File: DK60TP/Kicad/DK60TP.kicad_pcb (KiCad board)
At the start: 2 copper layers, 285.1 x 113.1 mm, 161 parts, among them J1 USB_mini_micro_B, K1 K00, K10 K09, K11 K0A, K12 K0B, K13 K0C, K14 K10, K15 K11, K16 K12, K17 K13, K18 K14, K19 K15, K2 K01, K20 K16, K21 K17, K22 K18, K23 K19, K24 K1A, K25 K1B, K26 K1C, K27 K20, K28 K21, K29 K22, K3 K02, K30 K23, K31 K24, K32 K25, K33 K26, K34 K27, K35 K28, K36 K29, K37 K2A, K38 K2B, K39 K2C, K4 K03, K40 K30, K41 K31, K42 K32, K43 K33, K44 K34, K45 K35, K46 K36, K47 K37, K48 K38, K49 K39, K5 K04, K50 K3A, K51 K3B, K52 K3C, K53 K41, K54 K42, K55 K45, K56 K48, K57 K49, K58 K4A, K59 K4B, K6 K05, K60 K4C, K61 Ctrl, K62 K43, K63 K44, K64 K46, K65 K45, K7 K06, K8 K07, K9 K08, SW1 SW_PUSH, U0 ATMEGA32U4, X1 XTAL_GND

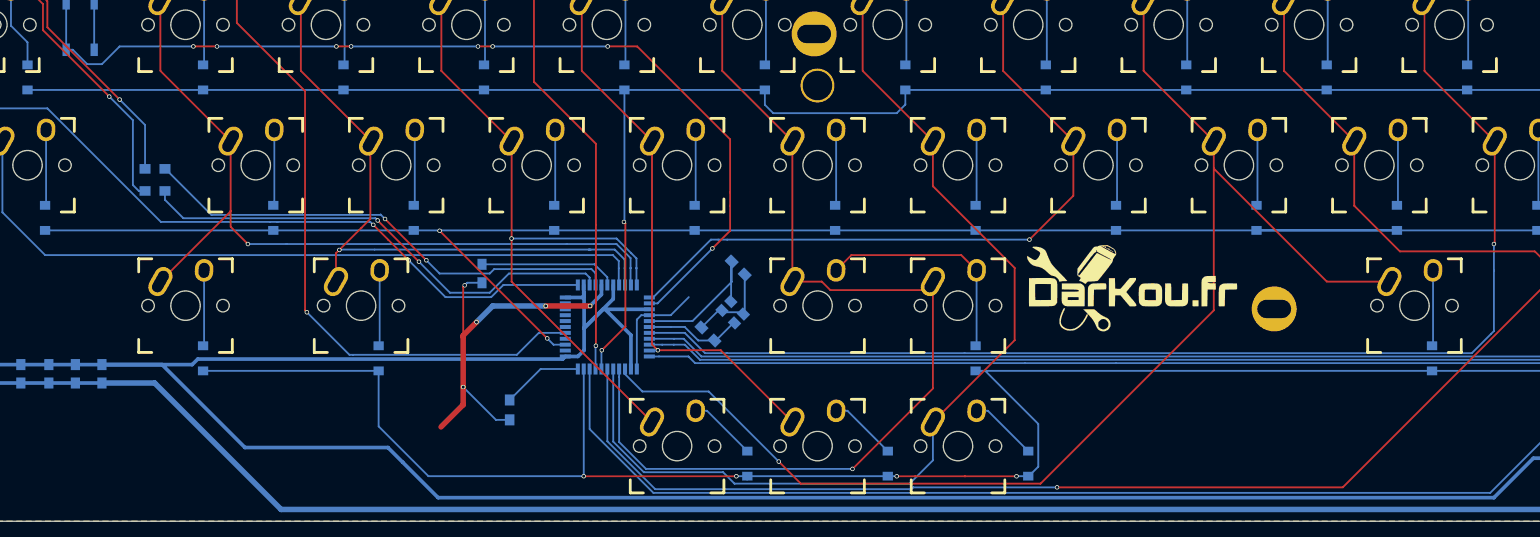
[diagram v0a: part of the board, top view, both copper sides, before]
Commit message: - DK60TP: Changed rows/cols assignation to  simplify routing
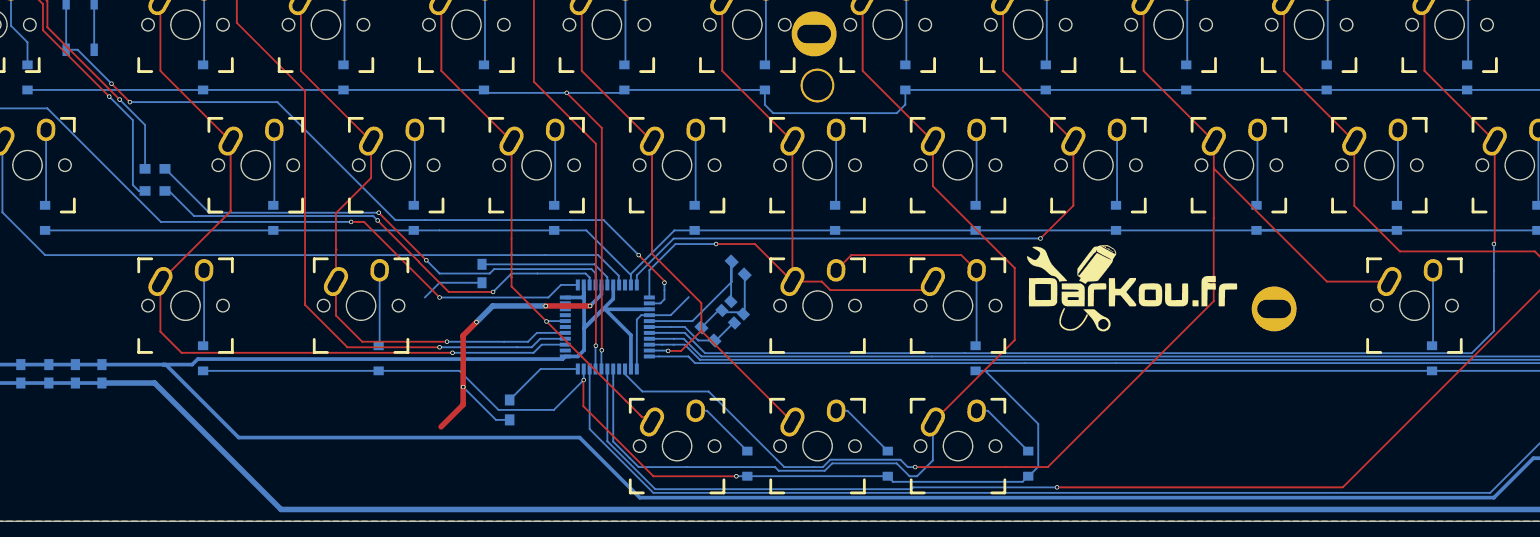
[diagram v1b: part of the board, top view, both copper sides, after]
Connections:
- U0 pad 10: /Col1 -> /Row3
- U0 pad 11: /Col3 -> /Col7
- U0 pad 12: /Col7 -> /Col5
- U0 pad 26: /Col5 -> Net-(U0-Pad26)
- U0 pad 36: /Row3 -> /Col1
- U0 pad 37: Net-(U0-Pad37) -> /Row0
- U0 pad 38: /Row0 -> /Col2
- U0 pad 40: Net-(U0-Pad40) -> /Col3
- U0 pad 9: /Col2 -> Net-(U0-Pad9)
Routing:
- net /Col5: track 179.1 -> 133.3 mm
- net Net-(R1-Pad2): track 136.9 -> 111.3 mm, vias 8 -> 4
- net /Col3: track 134.7 -> 116.0 mm
- net /Row3: track 291.3 -> 274.2 mm, vias 2 -> 0
- net /Row4: track 374.0 -> 362.4 mm, vias 4 -> 2
- net VCC: track 489.8 -> 481.5 mm
- net /Col2: track 131.1 -> 126.0 mm
- net /Col7: track 137.6 -> 140.3 mm
- net /Col4: track 119.2 -> 121.2 mm
- net /Col8: track 216.6 -> 214.8 mm
- net /Row0: track 351.1 -> 349.4 mm
- net /Col1: track 151.9 -> 153.4 mm
- net /Col0: track 161.3 -> 160.2 mm
- net GND: track 447.2 -> 446.2 mm, vias 12 -> 11
- net Net-(R3-Pad1): track 66.3 -> 65.6 mm

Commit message: - Rewrote all for DK60TP
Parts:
- removed D20: D16, Footprint:D_SOD123
- removed D25: D1B, Footprint:D_SOD123
- removed D30: D23, Footprint:D_SOD123
- removed G*** (x2): LOGO, Footprint:darkou
- removed G***: LOGO, Footprint:OPEN-HARDWARE
- removed K25: K1B, Footprint:Mx_Alps_100
- removed K26: K1C, Footprint:Mx_Alps_100
- removed K31: K24, Footprint:Mx_Alps_100
- removed K36: K29, Footprint:Mx_Alps_100
- removed K37: K2A, Footprint:Mx_Alps_100
- removed P?: CONN_1, Footprint:PIN_1
- removed the Poker_oval_hole at (91.8, 127.4)
- removed the Poker_oval_hole at (194.8, 146.5)
- removed the Poker_oval_hole at (326.8, 127.5)
- removed the Poker_oval_hole at (257.2, 183.8)
- removed the Poker_side_edge_long at (351.7, 156.0)
- removed the Poker_side_edge_long at (66.6, 156.0)
- added D64: D, Footprint:D_SOD123, B.Cu at (296.5, 38.0)
- added D65: D, Footprint:D_SOD123, B.Cu at (289.2, 58.8)
- added D66: D, Footprint:D_SOD123, B.Cu at (294.5, 77.5)
- added D67: D, Footprint:D_SOD123, B.Cu at (307.5, 95.0)
- added D68: D, Footprint:D_SOD123, B.Cu at (309.0, 111.8)
- added K66: K1B, Footprint:Mx_Alps_100, F.Cu at (257.2, 50.0)
- added K67: K2B, Footprint:Mx_Alps_100, F.Cu at (261.9, 69.1)
- added K68: K3B, Footprint:Mx_Alps_100, F.Cu at (252.4, 88.1)
- added K69: K4B, Footprint:Mx_Alps_100, F.Cu at (257.2, 107.2)
- added K70: K4B, Footprint:Mx_Alps_125, F.Cu at (254.8, 107.2)
- added K71: K4B, Footprint:Mx_Alps_150, F.Cu at (252.4, 107.2)
- added K72: K0C, Footprint:Mx_Alps_100, F.Cu at (266.7, 31.0)
- added K73: K1C, Footprint:Mx_Alps_100, F.Cu at (276.2, 50.0)
- added K74: K2C, Footprint:Mx_Alps_100, F.Cu at (281.0, 69.1)
- added K75: K3C, Footprint:Mx_Alps_275, F.Cu at (288.1, 88.1)
- added K76: K4C, Footprint:Mx_Alps_100, F.Cu at (276.2, 107.2)
- added K77: K4C, Footprint:Mx_Alps_125, F.Cu at (278.6, 107.2)
- added K78: K0D, Footprint:Mx_Alps_100, F.Cu at (285.8, 31.0)
- added K79: K0D, Footprint:Mx_Alps_200, F.Cu at (295.3, 31.0)
- added K80: K1D, Footprint:Mx_Alps_150, F.Cu at (300.0, 50.0)
- added K81: K2D, Footprint:Mx_Alps_225, F.Cu at (292.9, 69.1)
- added K82: K1D, Footprint:Mx_Alps_200, F.Cu at (302.4, 59.5)
- added K83: K3D, Footprint:Mx_Alps_100, F.Cu at (304.8, 88.1)
- added K84: K3C, Footprint:Mx_Alps_175, F.Cu at (278.6, 88.1)
- added K85: K4D, Footprint:Mx_Alps_125, F.Cu at (302.4, 107.2)
- added K86: K4D, Footprint:Mx_Alps_150, F.Cu at (300.0, 107.2)
- added MXST: VAL**, Footprint:MXST, F.Cu at (114.3, 107.2)
- added MXST: VAL**, Footprint:MXST, F.Cu at (304.8, 69.1)
- added MXST: VAL**, Footprint:MXST, F.Cu at (307.2, 31.0)
- added MXST: VAL**, Footprint:MXST, F.Cu at (283.4, 31.0)
- added MXST: VAL**, Footprint:MXST, F.Cu at (61.9, 88.1)
- added MXST: VAL**, Footprint:MXST, F.Cu at (38.1, 88.1)
- added MXST: VAL**, Footprint:MXST, F.Cu at (228.6, 107.2)
- added MXST: VAL**, Footprint:MXST, F.Cu at (209.6, 107.2)
- added MXST: VAL**, Footprint:MXST, F.Cu at (109.5, 107.2)
- added MXST: VAL**, Footprint:MXST, F.Cu at (300.0, 88.1)
- added MXST: VAL**, Footprint:MXST, F.Cu at (276.2, 88.1)
- added MXST: VAL**, Footprint:MXST, F.Cu at (302.4, 47.6)
- added MXST: VAL**, Footprint:MXST, F.Cu at (302.4, 71.4)
- added MXST: VAL**, Footprint:MXST, F.Cu at (281.0, 69.1)
- added P1: CONN_01X04, Pin_Headers:Pin_Header_Angled_1x04, B.Cu at (202.8, 104.8)
- added Poker_oval_hole: VAL**, Footprint:Poker_oval_hole, F.Cu at (289.1, 49.8)
- added Poker_oval_hole: VAL**, Footprint:Poker_oval_hole, F.Cu at (157.2, 68.9)
- added Poker_oval_hole: VAL**, Footprint:Poker_oval_hole, F.Cu at (219.5, 107.1)
- added Poker_side_edge_long: VAL**, Footprint:Poker_side_edge_long, F.Cu at (314.0, 78.4)
- added Poker_side_edge_long: VAL**, Footprint:Poker_side_edge_long, F.Cu at (29.0, 78.4)
- added REF**: MountingHole_2.2mm_M2_Pad, Mounting_Holes:MountingHole_2.2mm_M2_Pad, F.Cu at (157.2, 78.6)
- added REF**: MountingHole_2.2mm_M2_Pad, Mounting_Holes:MountingHole_2.2mm_M2_Pad, F.Cu at (54.2, 49.8)
- D1: value D00 -> D
- D10: value D09 -> D
- D11: value D0A -> D
- D12: value D0B -> D
- D13: value D0C -> D
- D14: value D10 -> D
- D15: value D11 -> D
- D16: value D12 -> D
- D17: value D13 -> D
- D18: value D14 -> D
- D19: value D15 -> D
- D2: value D01 -> D
- D21: value D17 -> D
- D22: value D18 -> D
- D23: value D19 -> D
- D24: value D1A -> D
- D26: value D1C -> D
- D27: value D20 -> D
- D28: value D21 -> D
- D29: value D22 -> D
- D3: value D02 -> D
- D31: value D24 -> D
- D32: value D25 -> D
- D33: value D26 -> D
- D34: value D27 -> D
- D35: value D28 -> D
- D36: value D29 -> D
- D37: value D2A -> D
- D38: value D2B -> D
- D39: value D2C -> D
- D4: value D03 -> D
- D40: value D30 -> D
- D41: value D31 -> D
- D42: value D32 -> D
- D43: value D33 -> D
- D44: value D34 -> D
- D45: value D35 -> D
- D46: value D36 -> D
- D47: value D37 -> D
- D48: value D38 -> D
- D49: value D39 -> D
- D5: value D04 -> D
- D50: value D3A -> D
- D51: value D3B -> D
- D52: value D3C -> D
- D53: value D41 -> D
- D54: value D42 -> D
- D55: value D45 -> D
- D56: value D48 -> D
- D57: value D49 -> D
- D58: value D4A -> D
- D59: value D4B -> D
- D6: value D05 -> D
- D60: value D4C -> D
- D61: value D43 -> D
- D62: value D44 -> D
- D63: value D46 -> D
- D7: value D06 -> D
- D8: value D07 -> D
- D9: value D08 -> D
- K10: value K09 -> K11
- K11: value K0A -> K21
- K12: value K0B -> K31
- K13: value K0C -> K41; footprint Footprint:Mx_Alps_100 -> Footprint:Mx_Alps_125
- K14: value K10 -> K41; footprint Footprint:Mx_Alps_150 -> Footprint:Mx_Alps_100
- K15: value K11 -> K02
- K17: value K13 -> K22
- K18: value K14 -> K32
- K19: value K15 -> K42; footprint Footprint:Mx_Alps_100 -> Footprint:Mx_Alps_125
- K2: value K01 -> K10; footprint Footprint:Mx_Alps_100 -> Footprint:Mx_Alps_150
- K20: value K16 -> K42; footprint Footprint:Mx_Alps_100 -> Footprint:Mx_Alps_150
- K21: value K17 -> K03
- K22: value K18 -> K13
- K23: value K19 -> K23
- K24: value K1A -> K33
- K27: value K20 -> K04; footprint Footprint:Mx_Alps_175 -> Footprint:Mx_Alps_100
- K28: value K21 -> K14
- K29: value K22 -> K24
- K3: value K02 -> K20; footprint Footprint:Mx_Alps_100 -> Footprint:Mx_Alps_175
- K30: value K23 -> K34
- K32: value K25 -> K05
- K33: value K26 -> K15
- K34: value K27 -> K25
- K35: value K28 -> K35
- K38: value K2B -> K06
- K39: value K2C -> K16; footprint Footprint:Mx_Alps_225 -> Footprint:Mx_Alps_100
- K4: value K03 -> K20; footprint Footprint:Mx_Alps_100 -> Footprint:Mx_Alps_175_STEPPED
- K40: value K30 -> K26; footprint Footprint:Mx_Alps_225 -> Footprint:Mx_Alps_100
- K41: value K31 -> K36
- K42: value K32 -> K46; footprint Footprint:Mx_Alps_100 -> Footprint:Mx_Alps_600
- K43: value K33 -> K46
- K44: value K34 -> K46; footprint Footprint:Mx_Alps_100 -> Footprint:Mx_Alps_625
- K45: value K35 -> K46; footprint Footprint:Mx_Alps_100 -> Footprint:Mx_Alps_700
- K46: value K36 -> K07
- K47: value K37 -> K17
- K48: value K38 -> K27
- K49: value K39 -> K37
- K5: value K04 -> K30; footprint Footprint:Mx_Alps_100 -> Footprint:Mx_Alps_225
- K50: value K3A -> K08
- K51: value K3B -> K18; footprint Footprint:Mx_Alps_175 -> Footprint:Mx_Alps_100
- K52: value K3C -> K28
- K53: value K41 -> K38
- K54: value K42 -> K09; footprint Footprint:Mx_Alps_150 -> Footprint:Mx_Alps_100
- K55: value K45 -> K19; footprint Footprint:Mx_Alps_600 -> Footprint:Mx_Alps_100
- K56: value K48 -> K29; footprint Footprint:Mx_Alps_150 -> Footprint:Mx_Alps_100
- K57: value K49 -> K39
- K58: value K4A -> K49
- K59: value K4B -> K0A
- K6: value K05 -> K30; footprint Footprint:Mx_Alps_100 -> Footprint:Mx_Alps_125
- K60: value K4C -> K1A; footprint Footprint:Mx_Alps_150 -> Footprint:Mx_Alps_100
- K61: value Ctrl -> K2A; footprint Footprint:Mx_Alps_175_STEPPED -> Footprint:Mx_Alps_100
- K62: value K43 -> K3A
- K63: value K44 -> K4A; footprint Footprint:Mx_Alps_100 -> Footprint:Mx_Alps_125
- K64: value K46 -> K4A; footprint Footprint:Mx_Alps_100 -> Footprint:Mx_Alps_150
- K65: value K45 -> K0B
- K7: value K06 -> K40; footprint Footprint:Mx_Alps_100 -> Footprint:Mx_Alps_125
- K8: value K07 -> K40; footprint Footprint:Mx_Alps_100 -> Footprint:Mx_Alps_150
- K9: value K08 -> K01
- moved K13 240.5 mm to (64.3, 107.2)
- moved K12 224.6 mm to (61.9, 88.1)
- moved D13 223.9 mm to (93.0, 76.0)
- moved D12 213.3 mm to (88.5, 57.0)
- moved D11 209.8 mm to (79.0, 38.0)
- moved D26 204.3 mm to (136.0, 38.0)
- moved K11 198.9 mm to (71.4, 69.1)
- moved K39 194.1 mm to (161.9, 50.0)
- moved D54 190.7 mm to (250.2, 38.0)
- moved K10 189.8 mm to (66.7, 50.0)
- moved K9 187.6 mm to (57.1, 31.0)
- moved K38 186.7 mm to (152.4, 31.0)
- moved K61 181.1 mm to (242.9, 69.1)
- moved D10 180.4 mm to (76.8, 107.2)
- moved K24 180.3 mm to (100.0, 88.1)
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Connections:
- D10 pad 1: /Row0 -> /Row4
- D12 pad 1: /Row0 -> /Row1
- D13 pad 1: /Row0 -> /Row2
- D14 pad 1: /Row1 -> /Row3
- D15 pad 1: /Row1 -> /Row4
- D16 pad 1: /Row1 -> /Row0
- D18 pad 1: /Row1 -> /Row2
- D19 pad 1: /Row1 -> /Row3
- D2 pad 1: /Row0 -> /Row1
- D21 pad 1: /Row1 -> /Row0
- D23 pad 1: /Row1 -> /Row2
- D24 pad 1: /Row1 -> /Row3
- D26 pad 1: /Row1 -> /Row0
- D27 pad 1: /Row2 -> /Row1
- D29 pad 1: /Row2 -> /Row3
- D3 pad 1: /Row0 -> /Row2
- D31 pad 1: /Row2 -> /Row0
- D32 pad 1: /Row2 -> /Row1
- D34 pad 1: /Row2 -> /Row3
- D35 pad 1: /Row2 -> /Row4
- D36 pad 1: /Row2 -> /Row0
- D37 pad 1: /Row2 -> /Row1
- D39 pad 1: /Row2 -> /Row3
- D4 pad 1: /Row0 -> /Row3
- D40 pad 1: /Row3 -> /Row0
- D41 pad 1: /Row3 -> /Row1
- D42 pad 1: /Row3 -> /Row2
- D44 pad 1: /Row3 -> /Row0
- D45 pad 1: /Row3 -> /Row1
- D46 pad 1: /Row3 -> /Row2
- D48 pad 1: /Row3 -> /Row4
- D49 pad 1: /Row3 -> /Row0
- D5 pad 1: /Row0 -> /Row4
- D50 pad 1: /Row3 -> /Row1
- D51 pad 1: /Row3 -> /Row2
- D54 pad 1: /Row4 -> /Row0
- D55 pad 1: /Row4 -> /Row1
- D56 pad 1: /Row4 -> /Row2
- D57 pad 1: /Row4 -> /Row3
- D59 pad 1: /Row4 -> /Row0
- D60 pad 1: /Row4 -> /Row1
- D61 pad 1: /Row4 -> /Row2
- D62 pad 1: /Row4 -> /Row3
- D7 pad 1: /Row0 -> /Row1
- D8 pad 1: /Row0 -> /Row2
- D9 pad 1: /Row0 -> /Row3
- K10 pad 1: /Col9 -> /Col1
- K10 pad 2: Net-(D10-Pad2) -> Net-(D7-Pad2)
- K11 pad 1: /Col10 -> /Col1
- K11 pad 2: Net-(D11-Pad2) -> Net-(D8-Pad2)
- K12 pad 1: /Col11 -> /Col1
- K12 pad 2: Net-(D12-Pad2) -> Net-(D9-Pad2)
- K13 pad 1: /Col12 -> /Col1
- K13 pad 2: Net-(D13-Pad2) -> Net-(D10-Pad2)
- K14 pad 1: /Col0 -> /Col1
- K14 pad 2: Net-(D14-Pad2) -> Net-(D10-Pad2)
- K15 pad 1: /Col1 -> /Col2
- K15 pad 2: Net-(D15-Pad2) -> Net-(D11-Pad2)
- K16 pad 2: Net-(D16-Pad2) -> Net-(D12-Pad2)
- K17 pad 1: /Col3 -> /Col2
- K17 pad 2: Net-(D17-Pad2) -> Net-(D13-Pad2)
- K18 pad 1: /Col4 -> /Col2
- K18 pad 2: Net-(D18-Pad2) -> Net-(D14-Pad2)
- K19 pad 1: /Col5 -> /Col2
- K19 pad 2: Net-(D19-Pad2) -> Net-(D15-Pad2)
- K2 pad 1: /Col1 -> /Col0
- K20 pad 1: /Col6 -> /Col2
- K20 pad 2: Net-(D20-Pad2) -> Net-(D15-Pad2)
- K21 pad 1: /Col7 -> /Col3
- K21 pad 2: Net-(D21-Pad2) -> Net-(D16-Pad2)
- K22 pad 1: /Col8 -> /Col3
- K22 pad 2: Net-(D22-Pad2) -> Net-(D17-Pad2)
- K23 pad 1: /Col9 -> /Col3
- K23 pad 2: Net-(D23-Pad2) -> Net-(D18-Pad2)
- K24 pad 1: /Col10 -> /Col3
- K24 pad 2: Net-(D24-Pad2) -> Net-(D19-Pad2)
- K27 pad 1: /Col0 -> /Col4
- K27 pad 2: Net-(D27-Pad2) -> Net-(D21-Pad2)
- K28 pad 1: /Col1 -> /Col4
- K28 pad 2: Net-(D28-Pad2) -> Net-(D22-Pad2)
- K29 pad 1: /Col2 -> /Col4
- K29 pad 2: Net-(D29-Pad2) -> Net-(D23-Pad2)
- K3 pad 1: /Col2 -> /Col0
- K30 pad 1: /Col3 -> /Col4
- K30 pad 2: Net-(D30-Pad2) -> Net-(D24-Pad2)
- K32 pad 2: Net-(D32-Pad2) -> Net-(D26-Pad2)
- K33 pad 1: /Col6 -> /Col5
- K33 pad 2: Net-(D33-Pad2) -> Net-(D27-Pad2)
- K34 pad 1: /Col7 -> /Col5
- K34 pad 2: Net-(D34-Pad2) -> Net-(D28-Pad2)
- K35 pad 1: /Col8 -> /Col5
- K35 pad 2: Net-(D35-Pad2) -> Net-(D29-Pad2)
- K38 pad 1: /Col11 -> /Col6
- K38 pad 2: Net-(D38-Pad2) -> Net-(D31-Pad2)
- K39 pad 1: /Col12 -> /Col6
- K39 pad 2: Net-(D39-Pad2) -> Net-(D32-Pad2)
- K4 pad 1: /Col3 -> Net-(D3-Pad2)
- K4 pad 2: Net-(D4-Pad2) -> /Col0
- K40 pad 1: /Col0 -> /Col6
- K40 pad 2: Net-(D40-Pad2) -> Net-(D33-Pad2)
- K41 pad 1: /Col1 -> /Col6
- K41 pad 2: Net-(D41-Pad2) -> Net-(D34-Pad2)
- K42 pad 1: /Col2 -> /Col6
- K42 pad 2: Net-(D42-Pad2) -> Net-(D35-Pad2)
- K43 pad 1: /Col3 -> /Col6
- K43 pad 2: Net-(D43-Pad2) -> Net-(D35-Pad2)
- K44 pad 1: /Col4 -> /Col6
- K44 pad 2: Net-(D44-Pad2) -> Net-(D35-Pad2)
- K45 pad 1: /Col5 -> Net-(D35-Pad2)
- K45 pad 2: Net-(D45-Pad2) -> /Col6
- K46 pad 1: /Col6 -> /Col7
- K46 pad 2: Net-(D46-Pad2) -> Net-(D36-Pad2)
- K47 pad 2: Net-(D47-Pad2) -> Net-(D37-Pad2)
- K48 pad 1: /Col8 -> /Col7
- K48 pad 2: Net-(D48-Pad2) -> Net-(D38-Pad2)
- K49 pad 1: /Col9 -> /Col7
- K49 pad 2: Net-(D49-Pad2) -> Net-(D39-Pad2)
- K5 pad 1: /Col4 -> /Col0
- K5 pad 2: Net-(D5-Pad2) -> Net-(D4-Pad2)
- K50 pad 1: /Col10 -> /Col8
- K50 pad 2: Net-(D50-Pad2) -> Net-(D40-Pad2)
- K51 pad 1: /Col11 -> /Col8
- K51 pad 2: Net-(D51-Pad2) -> Net-(D41-Pad2)
- K52 pad 1: /Col12 -> /Col8
- K52 pad 2: Net-(D52-Pad2) -> Net-(D42-Pad2)
- K53 pad 1: /Col1 -> /Col8
- K53 pad 2: Net-(D53-Pad2) -> Net-(D43-Pad2)
- K54 pad 1: /Col2 -> /Col9
- K54 pad 2: Net-(D54-Pad2) -> Net-(D44-Pad2)
- K55 pad 1: /Col5 -> /Col9
- K55 pad 2: Net-(D55-Pad2) -> Net-(D45-Pad2)
- K56 pad 1: /Col8 -> /Col9
- K56 pad 2: Net-(D56-Pad2) -> Net-(D46-Pad2)
- K57 pad 2: Net-(D57-Pad2) -> Net-(D47-Pad2)
- K58 pad 1: /Col10 -> /Col9
- K58 pad 2: Net-(D58-Pad2) -> Net-(D48-Pad2)
- K59 pad 1: /Col11 -> /ColA
- K59 pad 2: Net-(D59-Pad2) -> Net-(D49-Pad2)
- K6 pad 1: /Col5 -> /Col0
- K6 pad 2: Net-(D6-Pad2) -> Net-(D4-Pad2)
- K60 pad 1: /Col12 -> /ColA
- K60 pad 2: Net-(D60-Pad2) -> Net-(D50-Pad2)
- K61 pad 1: Net-(D27-Pad2) -> /ColA
- K61 pad 2: /Col0 -> Net-(D51-Pad2)
- K62 pad 1: /Col3 -> /ColA
- K62 pad 2: Net-(D61-Pad2) -> Net-(D52-Pad2)
- K63 pad 1: /Col4 -> /ColA
- K63 pad 2: Net-(D62-Pad2) -> Net-(D53-Pad2)
- K64 pad 1: /Col6 -> /ColA
- K64 pad 2: Net-(D63-Pad2) -> Net-(D53-Pad2)
- K65 pad 1: /Col5 -> /ColB
- K65 pad 2: Net-(D55-Pad2) -> Net-(D54-Pad2)
- K7 pad 1: /Col6 -> /Col0
- K7 pad 2: Net-(D7-Pad2) -> Net-(D5-Pad2)
- K8 pad 1: /Col7 -> /Col0
- K8 pad 2: Net-(D8-Pad2) -> Net-(D5-Pad2)
- K9 pad 1: /Col8 -> /Col1
- K9 pad 2: Net-(D9-Pad2) -> Net-(D6-Pad2)
- R2 pad 1: Net-(R2-Pad1) -> GND
- R2 pad 2: GND -> Net-(R2-Pad2)
- U0 pad 18: /Col10 -> /ColA
- U0 pad 19: /Col11 -> /ColB
- U0 pad 21: /Col4 -> /ColC
- U0 pad 30: /Row1 -> /Col4
- U0 pad 31: /Col12 -> /Row1
- U0 pad 33: Net-(R2-Pad1) -> Net-(R2-Pad2)
- U0 pad 36: /Col1 -> /Col0
- U0 pad 38: /Col2 -> /Col1
- U0 pad 39: Net-(U0-Pad39) -> /Col2
- U0 pad 43: Net-(U0-Pad43) -> GND
- U0 pad 8: /Col0 -> Net-(U0-Pad8)
- U0 pad 9: Net-(U0-Pad9) -> /ColD
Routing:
- net /Col12: track 319.0 -> 0.00 mm, vias 1 -> 0
- net /ColD: track 0.00 -> 302.2 mm, vias 0 -> 5
- net /Col10: track 289.4 -> 0.00 mm, vias 1 -> 0
- net /ColC: track 0.00 -> 286.3 mm, vias 0 -> 2
- net /Col11: track 283.8 -> 0.00 mm, vias 1 -> 0
- net /ColB: track 0.00 -> 277.7 mm, vias 0 -> 2
- net GND: track 446.2 -> 200.3 mm, vias 11 -> 10
- net /ColA: track 0.00 -> 239.5 mm, vias 0 -> 2
- net /Col3: track 116.0 -> 242.1 mm, vias 1 -> 2
- net Net-(C8-Pad1): track 18.8 -> 134.8 mm, vias 0 -> 4
- net /Col4: track 121.2 -> 232.5 mm, vias 1 -> 4
- net /Row0: track 349.4 -> 454.5 mm, vias 2 -> 0
- net VCC: track 481.5 -> 384.8 mm, vias 2 -> 6
- net D5: track 163.9 -> 88.5 mm, vias 1 -> 5
- net D2: track 153.6 -> 86.3 mm, vias 1 -> 6
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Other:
- board size 285.1 x 113.1 mm -> 285 x 94.5 mm
- board text removed: "DK60TP rev.A"

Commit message: - Added MouseButtons project - Updated DK60TP - Updated readme
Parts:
- removed P1: CONN_01X04, Pin_Headers:Pin_Header_Angled_1x04
- removed TP1: IBM_Trackpoint, Footprint:IBM_Trackpad
- added G***: LOGO, Footprint:darkou, B.Cu at (258.2, 94.0)
- added G***: LOGO, Footprint:darkou, F.Cu at (130.0, 107.2)
- added G***: LOGO, Footprint:OPEN-HARDWARE, B.Cu at (267.5, 55.8)
- added P2: CONN_02X05, Pin_Headers:Pin_Header_Angled_2x05, B.Cu at (203.0, 102.5)
- moved R8 23.2 mm to (189.5, 99.8), turned to 0 degrees
- moved R9 14.8 mm to (198.0, 99.2), turned to 0 degrees
- moved C9 4.93 mm to (188.8, 97.2)
- moved D35 3.20 mm to (179.8, 106.0), turned to 135 degrees
- moved R7 2.02 mm to (193.5, 99.0), turned to 270 degrees
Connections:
- net Net-(C9-Pad1) renamed TPRESET
- net VCC renamed TPVcc
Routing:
- net GND: track 200.3 -> 152.9 mm, vias 10 -> 12
- net TPRESET: track 7.60 -> 25.3 mm
- net (no net): track 16.6 -> 0.00 mm, vias 3 -> 0
- net D5: track 88.5 -> 83.5 mm, vias 5 -> 4
- net /Row4: track 381.6 -> 385.5 mm
- net /Col4: track 232.5 -> 228.9 mm
- net /Col8: track 149.9 -> 146.6 mm
- net Net-(D35-Pad2): track 39.2 -> 36.5 mm
- net D2: track 86.3 -> 83.8 mm, vias 6 -> 5
- net /Col9: track 278.7 -> 276.8 mm
- net /Col5: track 192.2 -> 193.6 mm
- net /CAPS_LED: track 131.6 -> 130.4 mm
- net Net-(D4-Pad2): track 21.5 -> 20.8 mm
- net /Col3: track 242.1 -> 241.6 mm
- net TPVcc: track 384.8 -> 385.4 mm, vias 6 -> 4
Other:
- board text added: "DK60TP Rev. A"

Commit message: - DK60TP: reducing quantity of VIAs
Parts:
- moved D53 22.3 mm to (222.0, 100.0), turned to 0 degrees
- moved D2 13.3 mm to (58.8, 58.5), turned to 180 degrees
- moved R6 12.6 mm to (37.8, 73.2), turned to 135 degrees
- moved D68 8.76 mm to (309.5, 103.0), turned to 225 degrees
- moved D43 8.05 mm to (206.5, 91.5)
- moved D34 7.94 mm to (166.8, 91.2)
- moved D52 7.60 mm to (242.8, 91.5)
- moved D57 7.38 mm to (261.5, 91.5)
- moved D39 7.29 mm to (185.2, 91.2)
- moved D47 6.95 mm to (223.0, 91.5)
- moved D62 6.31 mm to (296.0, 91.5)
- moved D63 6.18 mm to (286.2, 101.0), turned to 270 degrees
- moved D58 6.01 mm to (266.5, 101.0), turned to 270 degrees
- moved R8 5.55 mm to (184.0, 100.5)
- moved G*** 4.04 mm to (259.8, 97.8)
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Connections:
- net TPVcc renamed VCC
- C9 pad 1: TPRESET -> Net-(C9-Pad1)
- P2 pad 10: TPRESET -> D2
- P2 pad 3: /Col3 -> /Col5
- P2 pad 7: /Col5 -> /Col3
- P2 pad 8: D2 -> Net-(C9-Pad1)
- R7 pad 1: TPRESET -> Net-(C9-Pad1)
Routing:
- net TPRESET: track 25.3 -> 0.00 mm
- net Net-(C9-Pad1): track 0.00 -> 23.6 mm
- net /Row3: track 284.6 -> 263.7 mm
- net /CAPS_LED: track 130.4 -> 109.6 mm
- net /Row4: track 385.5 -> 367.0 mm
- net GND: track 152.9 -> 135.4 mm, vias 12 -> 10
- net /Row1: track 345.8 -> 328.9 mm
- net /Col3: track 241.6 -> 255.1 mm
- net Net-(D2-Pad2): track 10.1 -> 20.9 mm
- net Net-(D53-Pad2): track 10.9 -> 20.3 mm
- net Net-(D68-Pad2): track 15.3 -> 6.50 mm
- net Net-(LD1-Pad2): track 4.62 -> 12.2 mm
- net /Col7: track 143.8 -> 137.9 mm
- net VCC: track 385.4 -> 380.4 mm
- net D2: track 83.8 -> 88.5 mm, vias 5 -> 3
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
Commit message: - DK60TP: updated routing and reducing quantity of vias (again)
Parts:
- moved D53 17.1 mm to (239.0, 97.8), turned to 270 degrees
- moved LD1 8.14 mm to (31.2, 69.2)
- moved R6 8.06 mm to (44.8, 77.2), turned to 180 degrees
- moved R8 2.57 mm to (182.8, 98.2)
- moved D67 2.25 mm to (305.2, 95.0)
- moved D68 2.14 mm to (308.8, 101.0), turned to 270 degrees
- moved C9 2.02 mm to (188.2, 96.0), turned to 90 degrees
- moved R9 1.85 mm to (198.4, 96.4)
- moved D35 1.46 mm to (180.5, 104.8), turned to 180 degrees
- moved P2 1.20 mm to (202.9, 101.3)
- moved D29 1.03 mm to (147.2, 90.2)
- moved D39 1.00 mm to (185.2, 90.2)
- moved D34 0.95 mm to (166.7, 90.3)
- moved R7 0.56 mm to (193.0, 97.5), turned to 270 degrees
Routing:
- net VCC: track 380.4 -> 477.7 mm
- net /Row1: track 328.9 -> 386.6 mm
- net GND: track 135.4 -> 170.1 mm
- net Net-(D53-Pad2): track 20.3 -> 7.93 mm
- net Net-(D65-Pad2): track 21.7 -> 30.6 mm
- net /Row4: track 367.0 -> 358.5 mm
- net /ColD: track 301.0 -> 309.4 mm, vias 3 -> 2
- net /Col5: track 190.6 -> 183.6 mm
- net /CAPS_LED: track 109.6 -> 104.7 mm
- net Net-(LD1-Pad2): track 12.2 -> 15.5 mm
- net /ColA: track 239.5 -> 236.5 mm
- net Net-(D58-Pad2): track 36.0 -> 38.8 mm
- net /ColB: track 277.7 -> 275.0 mm
- net /ColC: track 286.3 -> 283.8 mm
- net D5: track 84.9 -> 87.3 mm
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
